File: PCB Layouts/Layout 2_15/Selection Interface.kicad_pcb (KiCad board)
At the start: 4 copper layers, 110 x 90 mm, 132 parts, among them P1 CONN_01X02, P11 CONN_01X02, P12 CONN_01X02, P13 CONN_01X10, P14 CONN_01X02, P15 CONN_01X02, P16 CONN_01X02, P18 CONN_02X05, P2 CONN_01X02, P3 CONN_01X02, P4 CONN_01X02, P5 CONN_01X02, P6 CONN_02X10, P7 CONN_01X02, P8 CONN_02X04, P9 CONN_01X02

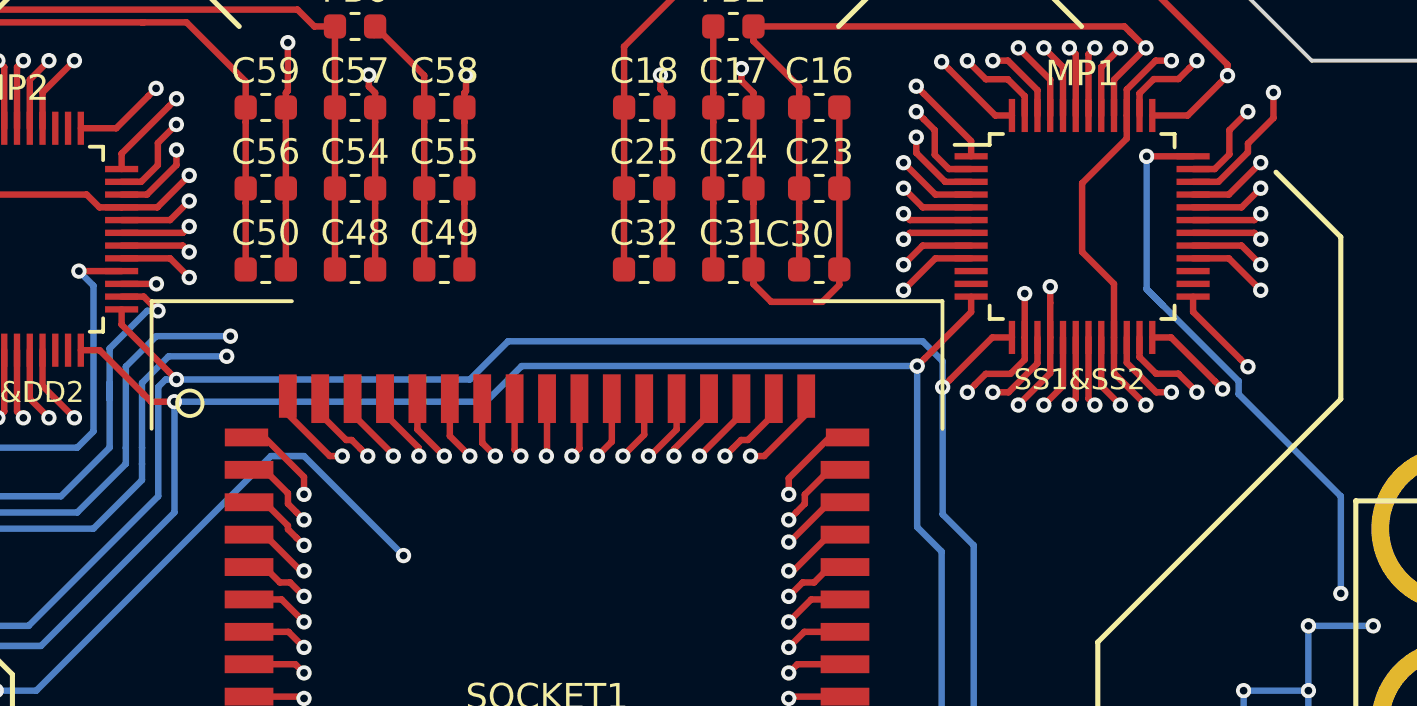
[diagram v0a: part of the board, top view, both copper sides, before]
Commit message: Added new schematic symbol for a new multiplexer processor that has more GPIO pins. Started modifying signal routing for the slightly different pinout
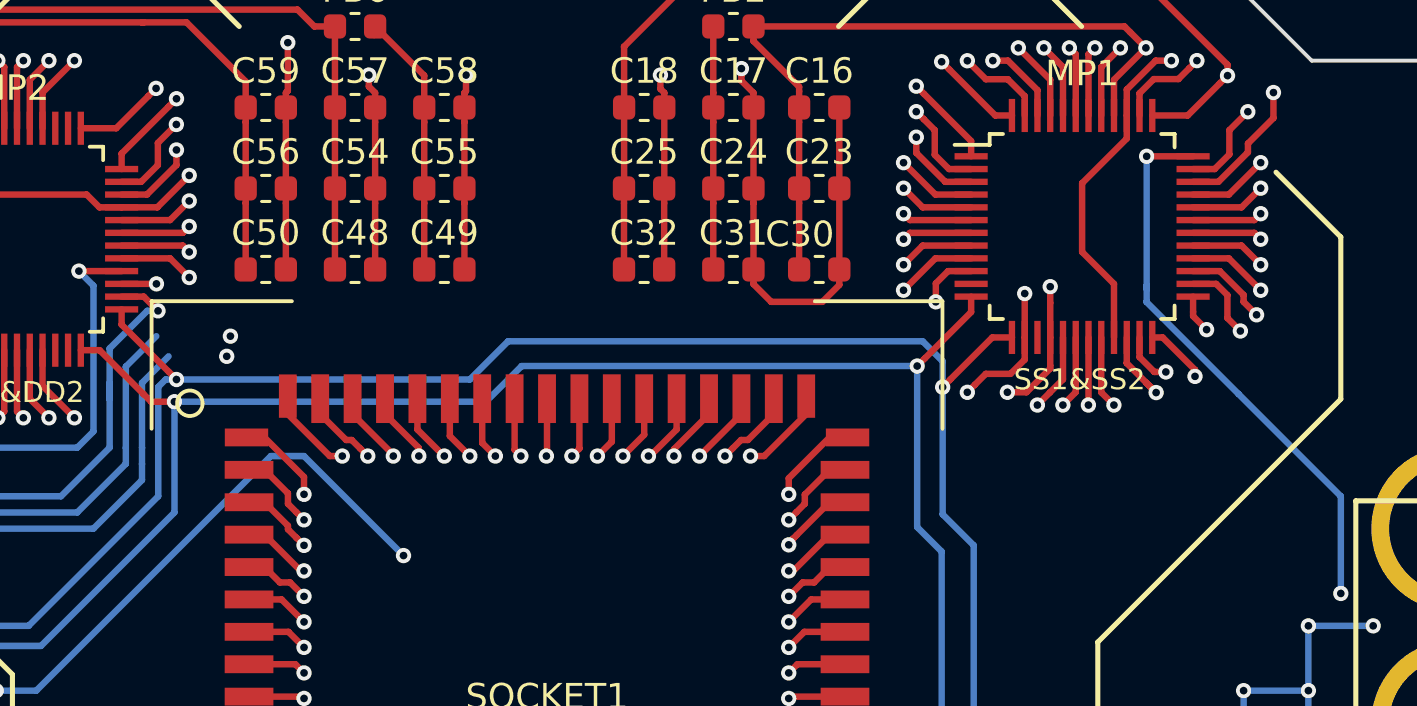
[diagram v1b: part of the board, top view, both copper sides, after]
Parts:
- MP1: value CY8C42_(48_TQFP) -> CY8C4245AZI-M433(48_TQPF)
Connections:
- MP1 pad 10: Net-(MP1-Pad10) -> GND
- MP1 pad 14: D17 -> SWDIO1
- MP1 pad 15: GND -> Net-(MP1-Pad15)
- MP1 pad 16: D18 -> SWDCLK1
- MP1 pad 17: D19 -> D17
- MP1 pad 18: D20 -> D18
- MP1 pad 19: D21 -> D19
- MP1 pad 20: D22 -> D20
- MP1 pad 22: D23 -> D21
- MP1 pad 23: D24 -> D22
- MP1 pad 24: D25 -> D23
- MP1 pad 25: D26 -> D24
- MP1 pad 26: Net-(MP1-Pad26) -> D25
- MP1 pad 27: Net-(MP1-Pad27) -> D26
- PROG2 pad 1: D18 -> SWDCLK1
- PROG2 pad 2: D17 -> SWDIO1
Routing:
- net SWDCLK1: track 0.00 -> 91.1 mm, vias 0 -> 5
- net D18: track 125.9 -> 48.1 mm, vias 7 -> 3
- net SWDIO1: track 0.00 -> 77.7 mm, vias 0 -> 5
- net D17: track 111.5 -> 42.9 mm, vias 7 -> 3
- net D20: track 48.6 -> 54.7 mm
- net D21: track 50.2 -> 54.7 mm
- net D19: track 47.5 -> 51.9 mm
- net D22: track 52.0 -> 55.3 mm
- net VDDD: track 305.4 -> 302.2 mm, vias 17 -> 16
- net D25: track 60.2 -> 63.1 mm
- net D26: track 64.1 -> 66.8 mm
- net D24: track 58.8 -> 61.0 mm
- net D23: track 56.4 -> 58.3 mm
- net D27: track 73.2 -> 74.1 mm
- net GND: track 611.2 -> 610.3 mm
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
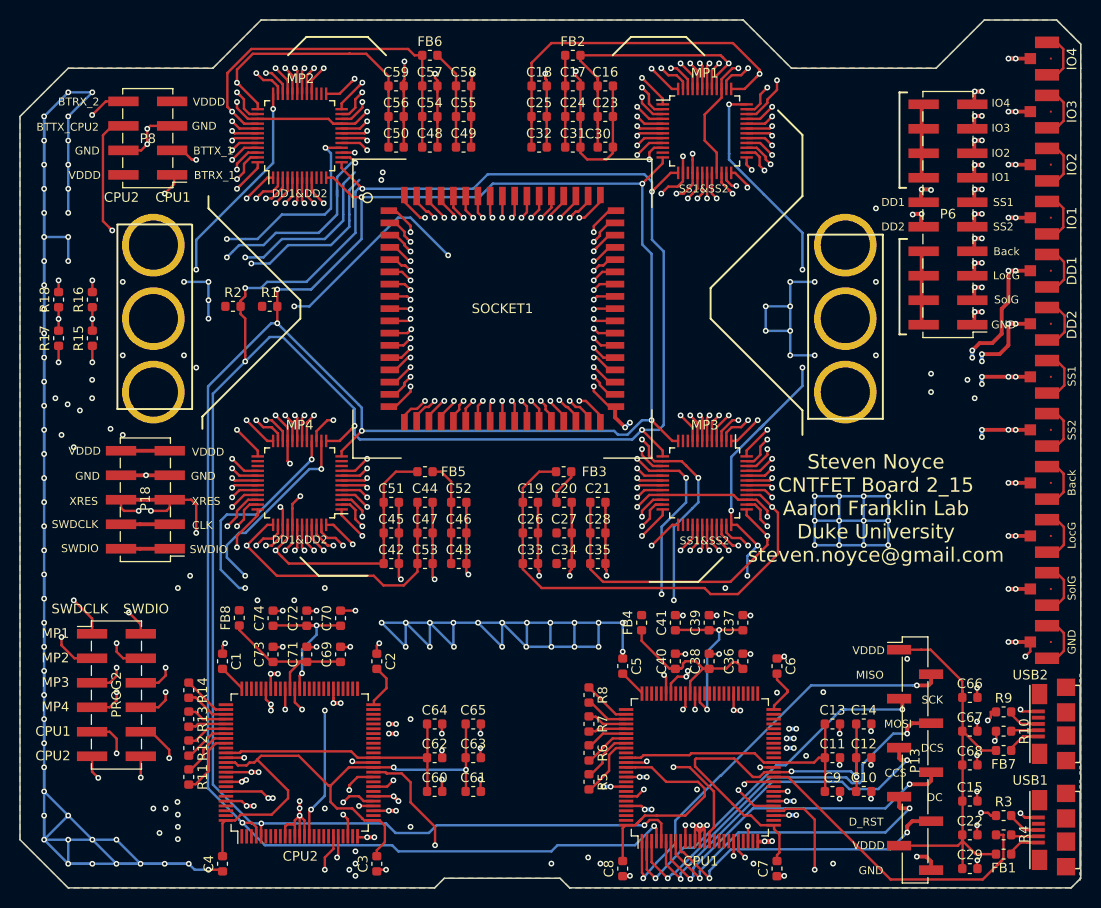
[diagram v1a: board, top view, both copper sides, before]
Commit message: Updated Red PCB layout so all MUXes fit the new pinout
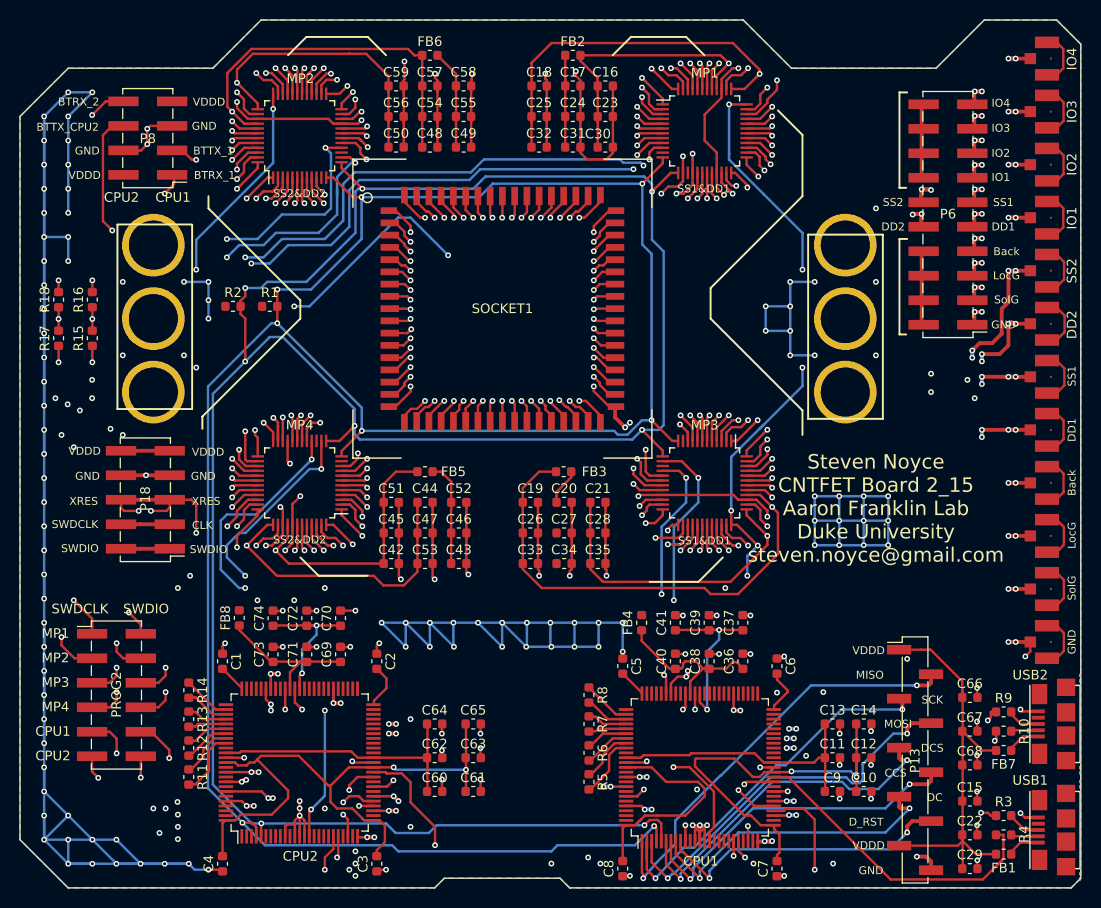
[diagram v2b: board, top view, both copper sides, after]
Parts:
- MP2, MP3, MP4: value CY8C42_(48_TQFP) -> CY8C4245AZI-M433(48_TQPF)
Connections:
- CPU1 pad 90: SS2 -> DD1
- CPU1 pad 96: DD1 -> SS2
- CPU2 pad 90: SS2 -> DD1
- CPU2 pad 96: DD1 -> SS2
- MP1 pad 35: SS2 -> DD1
- MP2 pad 10: Net-(MP2-Pad10) -> GND
- MP2 pad 15: GND -> Net-(MP2-Pad15)
- MP2 pad 17: D19 -> D17
- MP2 pad 18: D20 -> D18
- MP2 pad 19: D21 -> D19
- MP2 pad 20: D22 -> D20
- MP2 pad 22: D23 -> D21
- MP2 pad 23: D24 -> D22
- MP2 pad 24: D25 -> D23
- MP2 pad 25: D26 -> D24
- MP2 pad 26: Net-(MP2-Pad26) -> D25
- MP2 pad 27: Net-(MP2-Pad27) -> D26
- MP2 pad 34: DD1 -> SS2
- MP3 pad 10: Net-(MP3-Pad10) -> GND
- MP3 pad 14: D49 -> SWDIO3
- MP3 pad 15: GND -> Net-(MP3-Pad15)
- MP3 pad 16: D50 -> SWDCLK3
- MP3 pad 17: D51 -> D49
- MP3 pad 18: D52 -> D50
- MP3 pad 19: D53 -> D51
- MP3 pad 20: D54 -> D52
- MP3 pad 22: D55 -> D53
- MP3 pad 23: D56 -> D54
- MP3 pad 24: D57 -> D55
- MP3 pad 25: D58 -> D56
- MP3 pad 26: Net-(MP3-Pad26) -> D57
- MP3 pad 27: Net-(MP3-Pad27) -> D58
- MP3 pad 35: SS2 -> DD1
- MP4 pad 10: Net-(MP4-Pad10) -> GND
- MP4 pad 15: GND -> Net-(MP4-Pad15)
- MP4 pad 17: D51 -> D49
- MP4 pad 18: D52 -> D50
- MP4 pad 19: D53 -> D51
- MP4 pad 20: D54 -> D52
- MP4 pad 22: D55 -> D53
- MP4 pad 23: D56 -> D54
- MP4 pad 24: D57 -> D55
- MP4 pad 25: D58 -> D56
- MP4 pad 26: Net-(MP4-Pad26) -> D57
- MP4 pad 27: Net-(MP4-Pad27) -> D58
- MP4 pad 34: DD1 -> SS2
- P11 pad 1: DD1 -> SS2
- P5 pad 1: SS2 -> DD1
- P6 pad 12: DD1 -> SS2
- P6 pad 9: SS2 -> DD1
- PROG2 pad 5: D50 -> SWDCLK3
- PROG2 pad 6: D49 -> SWDIO3
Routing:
- net SS2: track 202.0 -> 290.2 mm, vias 13 -> 18
- net DD1: track 290.2 -> 202.0 mm, vias 18 -> 13
- net SWDIO3: track 0.00 -> 80.1 mm, vias 0 -> 4
- net SWDCLK3: track 0.00 -> 80.0 mm, vias 0 -> 4
- net D50: track 104.2 -> 49.3 mm, vias 6 -> 3
- net D49: track 103.8 -> 48.9 mm, vias 6 -> 3
- net SWDCLK1: track 91.1 -> 120.6 mm, vias 5 -> 6
- net SWDIO1: track 77.7 -> 106.6 mm, vias 5 -> 6
- net D18: track 48.1 -> 54.2 mm
- net D54: track 52.4 -> 58.4 mm
- net D17: track 42.9 -> 48.8 mm
- net D58: track 67.1 -> 72.4 mm
- net D22: track 55.3 -> 59.5 mm
- net D57: track 61.5 -> 65.5 mm
- net D53: track 50.4 -> 53.0 mm
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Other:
- board text added: "SS1&DD1"
- board text added: "SS2&DD2"
- board text removed: "DD1&DD2"
- board text removed: "SS1&SS2"

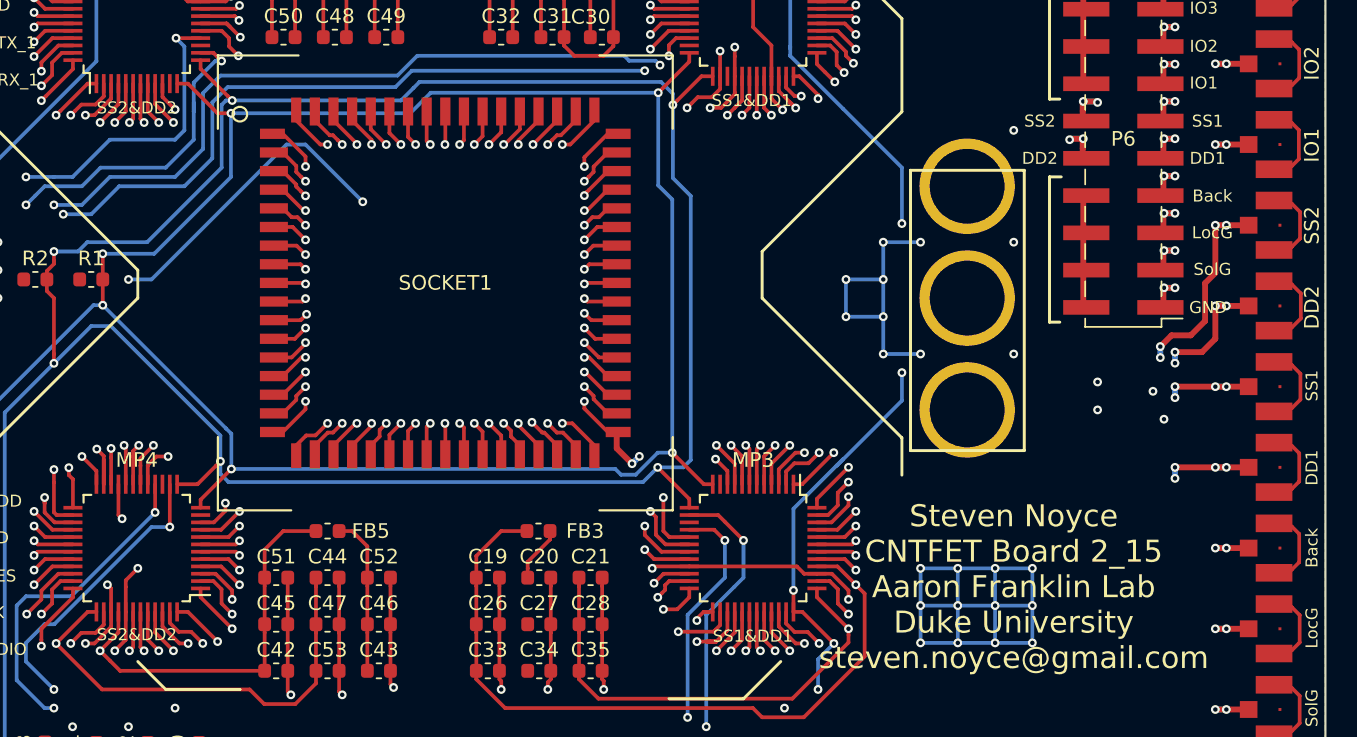
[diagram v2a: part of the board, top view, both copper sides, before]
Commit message: Reverted a signal-name change made on the layout. I realized it is impossible for a signle MUX to route the signals for SS1 and DD1. The source and drain would be shorted out if I tried to do that
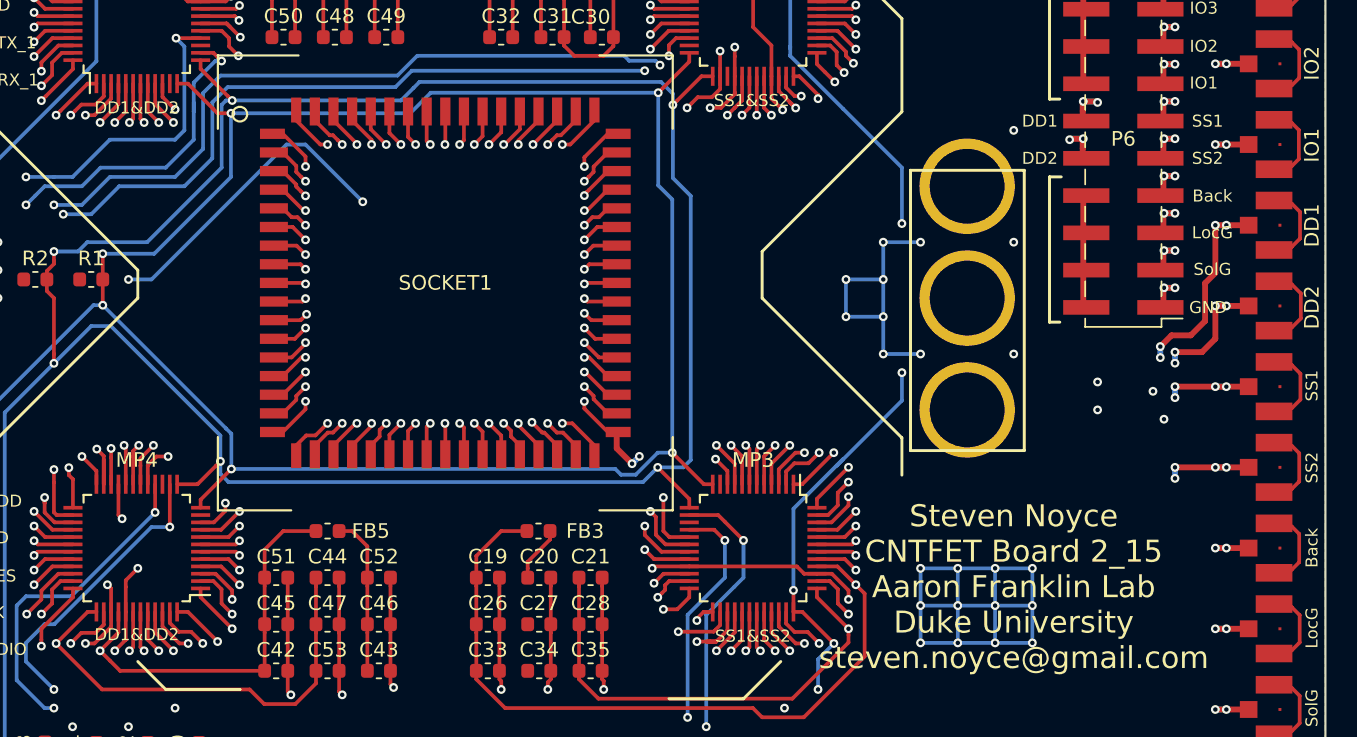
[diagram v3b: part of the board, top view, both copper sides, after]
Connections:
- CPU1 pad 90: DD1 -> SS2
- CPU1 pad 96: SS2 -> DD1
- CPU2 pad 90: DD1 -> SS2
- CPU2 pad 96: SS2 -> DD1
- MP1 pad 35: DD1 -> SS2
- MP2 pad 34: SS2 -> DD1
- MP3 pad 35: DD1 -> SS2
- MP4 pad 34: SS2 -> DD1
- P11 pad 1: SS2 -> DD1
- P5 pad 1: DD1 -> SS2
- P6 pad 12: SS2 -> DD1
- P6 pad 9: DD1 -> SS2
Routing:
- net SS2: track 290.2 -> 202.0 mm, vias 18 -> 13
- net DD1: track 202.0 -> 290.2 mm, vias 13 -> 18
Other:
- board text added: "DD1&DD2"
- board text added: "SS1&SS2"
- board text removed: "SS1&DD1"
- board text removed: "SS2&DD2"

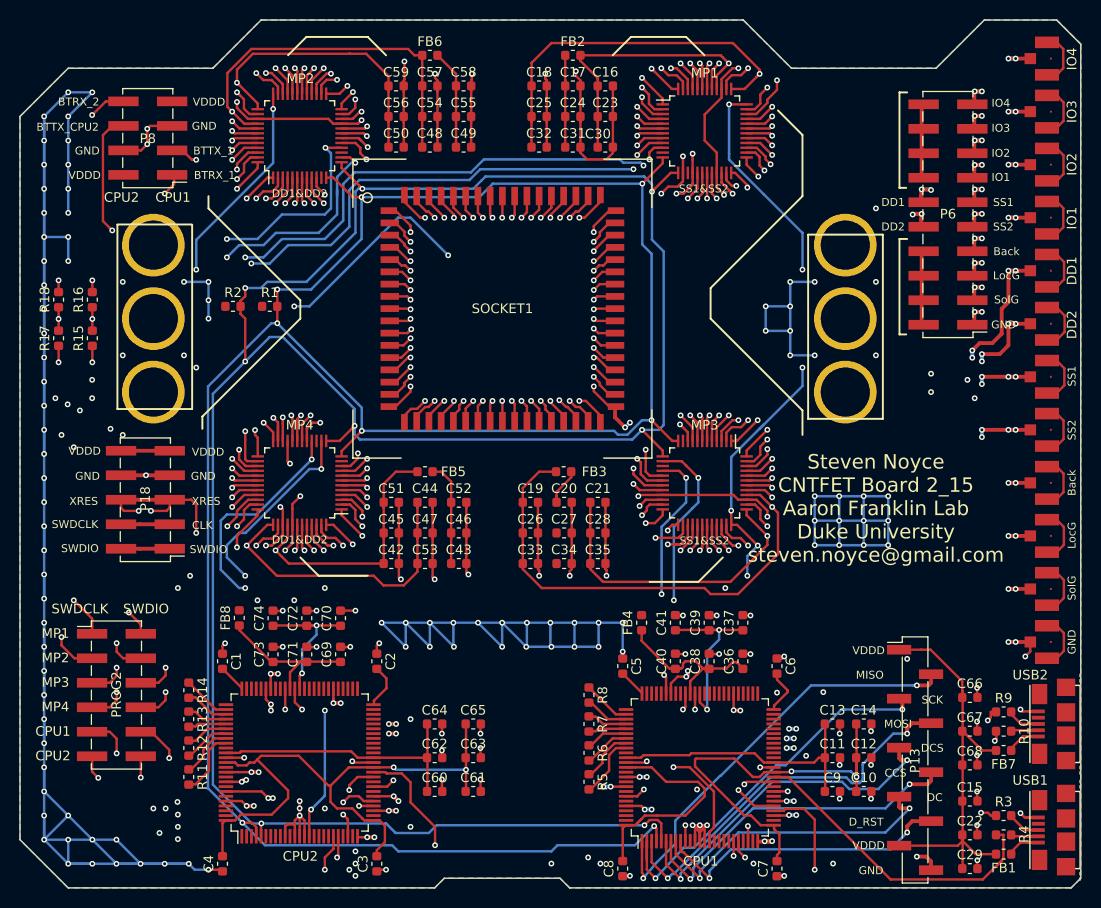
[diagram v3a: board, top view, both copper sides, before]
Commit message: Renamed device selectors to MUX1, MUX2, MUX3, MUX4
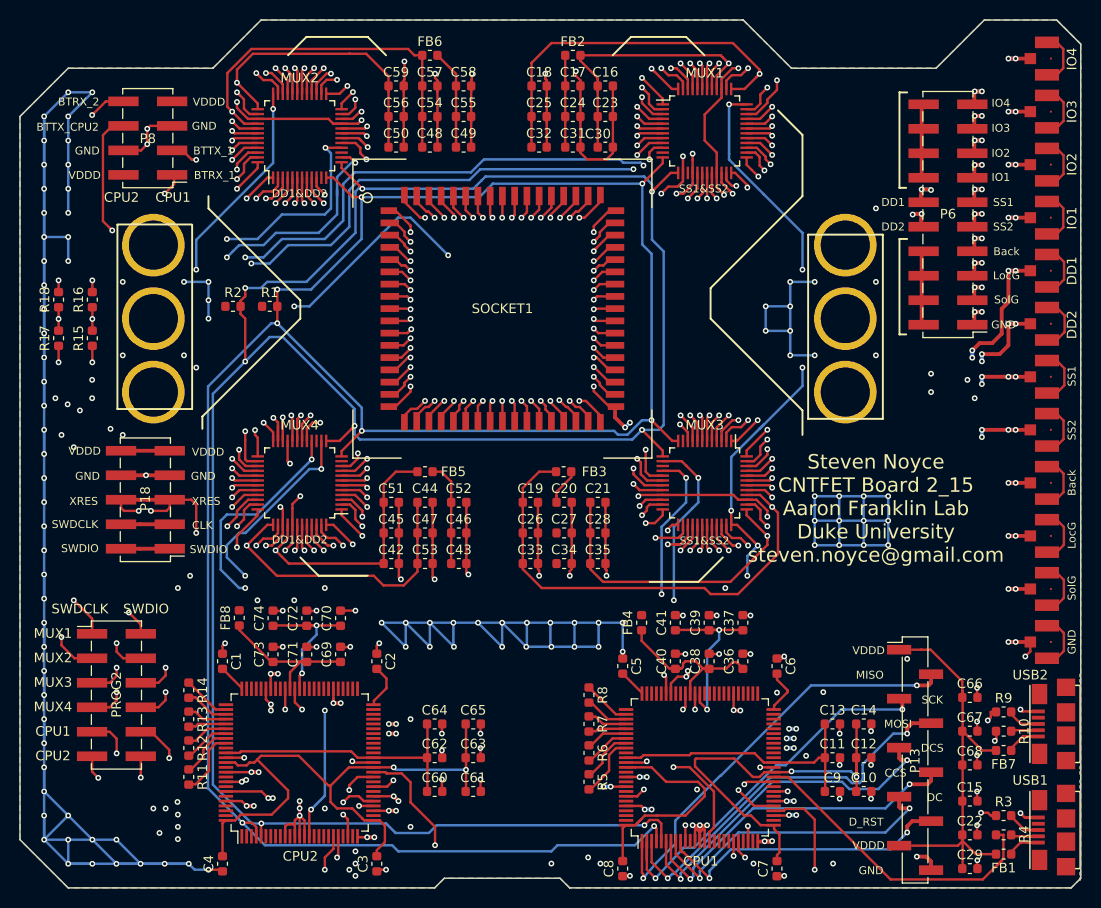
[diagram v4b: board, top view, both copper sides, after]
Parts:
- removed MP1, MP2, MP3, MP4: CY8C4245AZI-M433(48_TQPF), Package_QFP:TQFP-48_7x7mm_P0.5mm
- added MUX1: CY8C4245AZI-M433(48_TQPF), Package_QFP:TQFP-48_7x7mm_P0.5mm, F.Cu at (221.0, 81.5)
- added MUX2: CY8C4245AZI-M433(48_TQPF), Package_QFP:TQFP-48_7x7mm_P0.5mm, F.Cu at (179.0, 82.0)
- added MUX3: CY8C4245AZI-M433(48_TQPF), Package_QFP:TQFP-48_7x7mm_P0.5mm, F.Cu at (221.0, 118.0)
- added MUX4: CY8C4245AZI-M433(48_TQPF), Package_QFP:TQFP-48_7x7mm_P0.5mm, F.Cu at (179.0, 118.0)
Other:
- board text added: "MUX1"
- board text added: "MUX2"
- board text added: "MUX3"
- board text added: "MUX4"
- board text removed: "MP1"
- board text removed: "MP2"
- board text removed: "MP3"
- board text removed: "MP4"
